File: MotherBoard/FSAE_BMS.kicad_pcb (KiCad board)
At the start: 2 copper layers, 61 parts, among them IC501 BQ79600PWRQ1, J1 DM3AT-SF-PEJM5_40_, J201 Conn_ARM_SWD_TagConnect_TC2030, J301 1376357-3, U201 STM32F205RBTx, U401 LMR51430, U402 LMR51430, U601 PTCAN1462DRQ1, U602 PTCAN1462DRQ1, Y201 16 Mhz

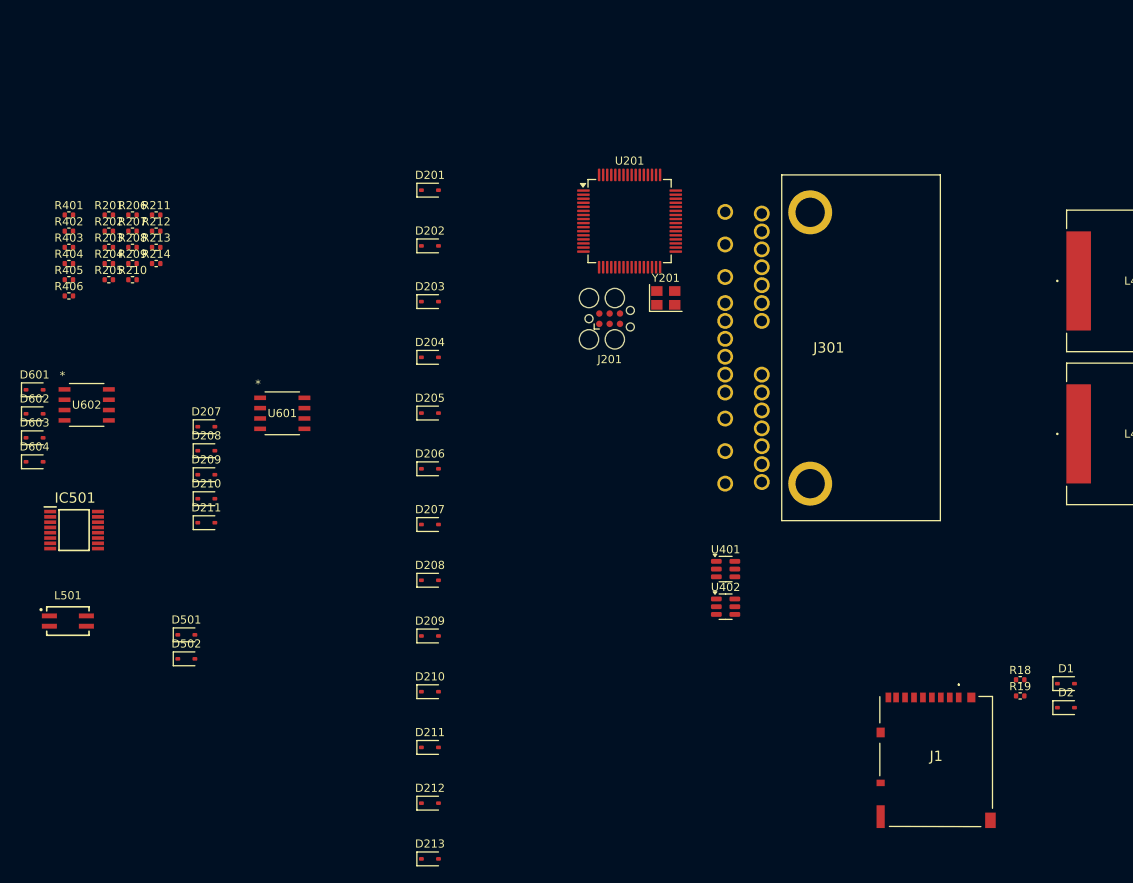
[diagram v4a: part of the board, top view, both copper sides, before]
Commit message: Revised all schematics + completed relay driver page
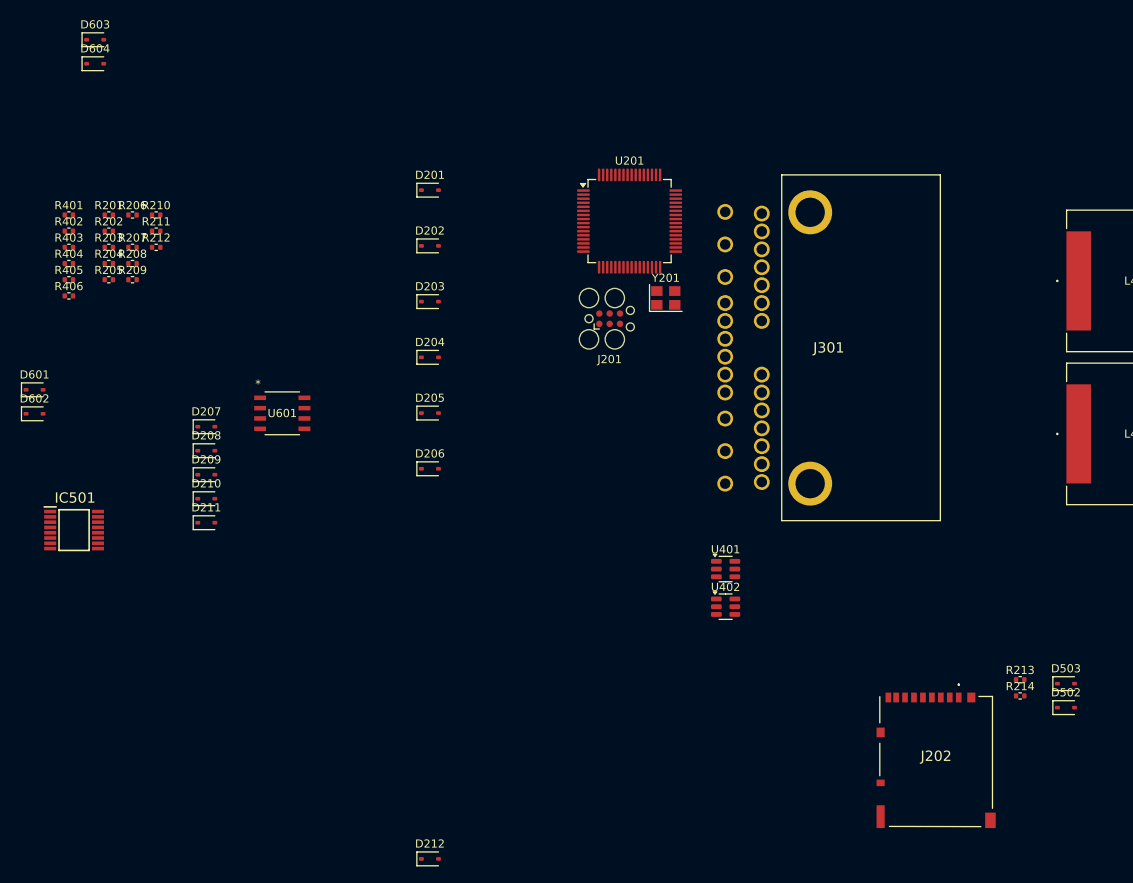
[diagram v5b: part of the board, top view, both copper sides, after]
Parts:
- removed the D207 at (89.1, 88.1)
- removed the D208 at (89.1, 95.0)
- removed the D209 at (89.1, 101.8)
- removed the D210 at (89.1, 108.7)
- removed the D211 at (89.1, 115.5)
- removed the D212 at (89.1, 122.4)
- removed D501: D_TVS, Diode_SMD:D_SOD-323
- removed the D502 at (59.2, 104.7)
- removed L501: WE-SLM, Transformer_WURTH:Isolation_Transformer
- removed the R207 at (52.5, 52.1)
- removed the R214 at (55.5, 56.1)
- removed U602: PTCAN1462DRQ1, TCAN:TCAN
- moved D603 49.5 mm to (48.0, 28.6)
- moved D604 49.5 mm to (48.0, 31.5)
- renumbered D213 to D212, D2 to D502, D1 to D503, J1 to J202, R208 to R207, R209 to R208, R210 to R209, R211 to R210, R212 to R211, R213 to R212, R18 to R213, R19 to R214
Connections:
- net Net-(U601-CANH) renamed /TCAN1462-Q1/CANH_1
- net Net-(U601-CANL) renamed /TCAN1462-Q1/CANL_1
- D502 pad 1: Net-(D1-A2) -> GND
- D503 pad 2: Net-(D1-A2) -> GND
- D601 pad 2: CAN1_CONN+ -> ISO_CAN1+
- D602 pad 1: CAN1_CONN- -> ISO_CAN1-
- D603 pad 2: CAN2_CONN+ -> ISO_CAN2+
- D604 pad 1: CAN2_CONN- -> ISO_CAN2-
- U201 pad 2: unconnected-(U201-PC13-Pad2) -> /MCU/SDIO_DET
- U201 pad 33: unconnected-(U201-PB12-Pad33) -> CAN2_RX
- U201 pad 34: unconnected-(U201-PB13-Pad34) -> CAN2_TX
- U201 pad 44: unconnected-(U201-PA11-Pad44) -> CAN1_RX
- U201 pad 45: unconnected-(U201-PA12-Pad45) -> CAN1_TX
- U201 pad 57: CAN2_RX -> unconnected-(U201-PB5-Pad57)
- U201 pad 58: CAN2_TX -> unconnected-(U201-PB6-Pad58)
- U201 pad 61: CAN1_RX -> unconnected-(U201-PB8-Pad61)
- U201 pad 62: CAN1_TX -> unconnected-(U201-PB9-Pad62)
- U601 pad 1: CAN1_TX -> Net-(U601-TXD)
- U601 pad 4: CAN1_RX -> Net-(U601-RXD)

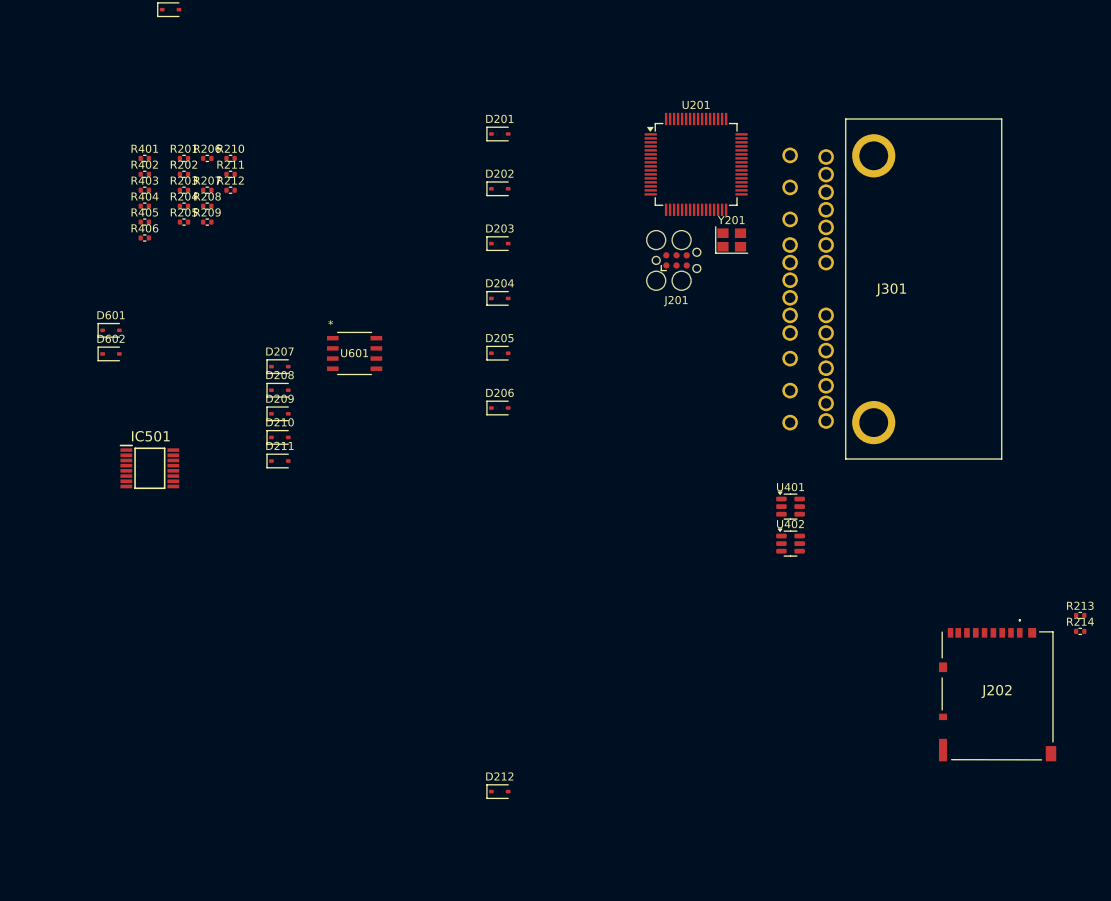
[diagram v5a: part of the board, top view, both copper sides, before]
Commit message: Fixed 3D model paths. Finished PSU ORing shcematic.
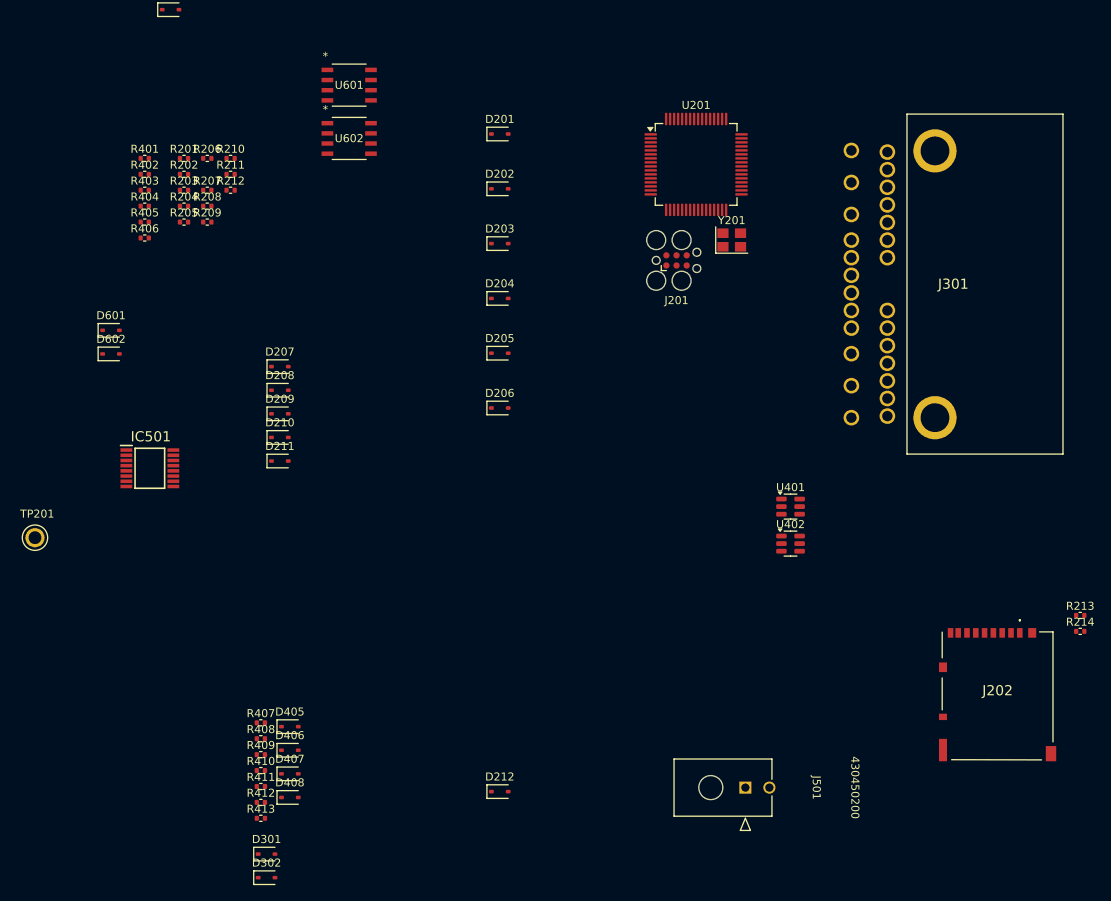
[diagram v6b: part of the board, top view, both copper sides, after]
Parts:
- added D301: D_TVS, Diode_SMD:D_SOD-323, F.Cu at (60.0, 137.1)
- added D302: D_TVS, Diode_SMD:D_SOD-323, F.Cu at (60.0, 140.0)
- added D405: D_TVS, Diode_SMD:D_SOD-323, F.Cu at (62.9, 121.1)
- added D406: D_TVS, Diode_SMD:D_SOD-323, F.Cu at (62.9, 124.1)
- added D407: D_TVS, Diode_SMD:D_SOD-323, F.Cu at (62.9, 127.0)
- added D408: D_TVS, Diode_SMD:D_SOD-323, F.Cu at (62.9, 130.0)
- added J501: 430450200, molex_comm:CON_430450200_MOL, F.Cu at (119.8, 128.7)
- added R407: 100k, Resistor_SMD:R_0402_1005Metric, F.Cu at (59.2, 120.6)
- added R408: 33k, Resistor_SMD:R_0402_1005Metric, F.Cu at (59.2, 122.6)
- added R409: 100k, Resistor_SMD:R_0402_1005Metric, F.Cu at (59.2, 124.6)
- added R410: 33k, Resistor_SMD:R_0402_1005Metric, F.Cu at (59.2, 126.6)
- added R411: 1k, Resistor_SMD:R_0402_1005Metric, F.Cu at (59.2, 128.6)
- added R412: 1k, Resistor_SMD:R_0402_1005Metric, F.Cu at (59.2, 130.6)
- added R413: 1K, Resistor_SMD:R_0402_1005Metric, F.Cu at (59.2, 132.6)
- added TP201: TestPoint, TestPoint:TP_5012, F.Cu at (31.0, 97.5)
- added U602: PTCAN1462DRQ1, CAN1462:CAN1462, F.Cu at (70.3, 47.6)
- U601: footprint TCAN:TCAN -> CAN1462:CAN1462
- moved U601 33.5 mm to (70.3, 40.9)
- moved J301 7.68 mm to (133.1, 49.1)
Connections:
- net CHARGE_EN_CONN renamed CHARGE_EN_HV
- net CHARGE_PWR_CONN renamed CHARGE_PWR
- net CHARGE_SAFE_CONN renamed CHARGE_SAFE_HV
- net DISCHARGE_EN_CONN renamed DISCHARGE_EN_HV
- net FAN_EN renamed FAN_EN_LV
- net FAN_EN_CONN renamed FAN_EN_HV
- net READY_PWR_CONN renamed READY_PWR
- J301 pad 18: CAN1_CONN+ -> ISO_CAN1+
- J301 pad 19: CAN1_CONN- -> ISO_CAN1-
- J301 pad 20: CAN2_CONN- -> ISO_CAN2+
- J301 pad 21: CAN2_CONN+ -> ISO_CAN2-
- J301 pad 24: FAN_PWM_CONN -> unconnected-(J301-Pad24)
- U201 pad 14: ADC3_IN0 -> unconnected-(U201-PA0-Pad14)
- U201 pad 15: ADC3_IN1 -> unconnected-(U201-PA1-Pad15)
- U201 pad 27: CHARGE_PWR_CTRL -> CHARGE_PWR_LV_ISO
- U201 pad 28: READY_PWR_CTRL -> READY_PWR_LV_ISO

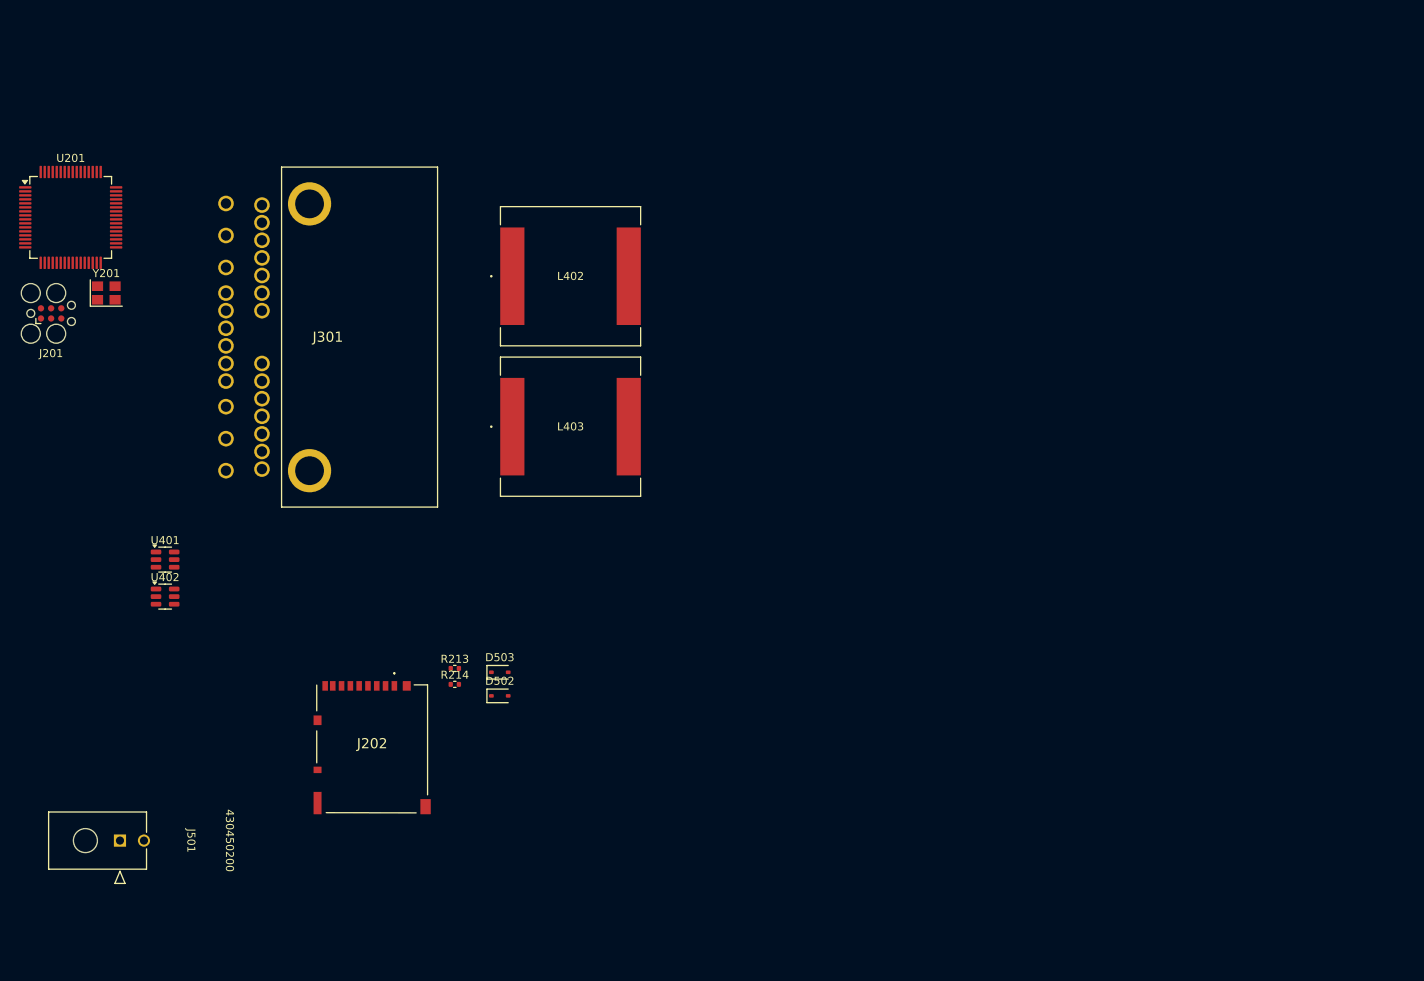
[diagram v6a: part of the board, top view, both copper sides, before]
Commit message: Added more 3D models
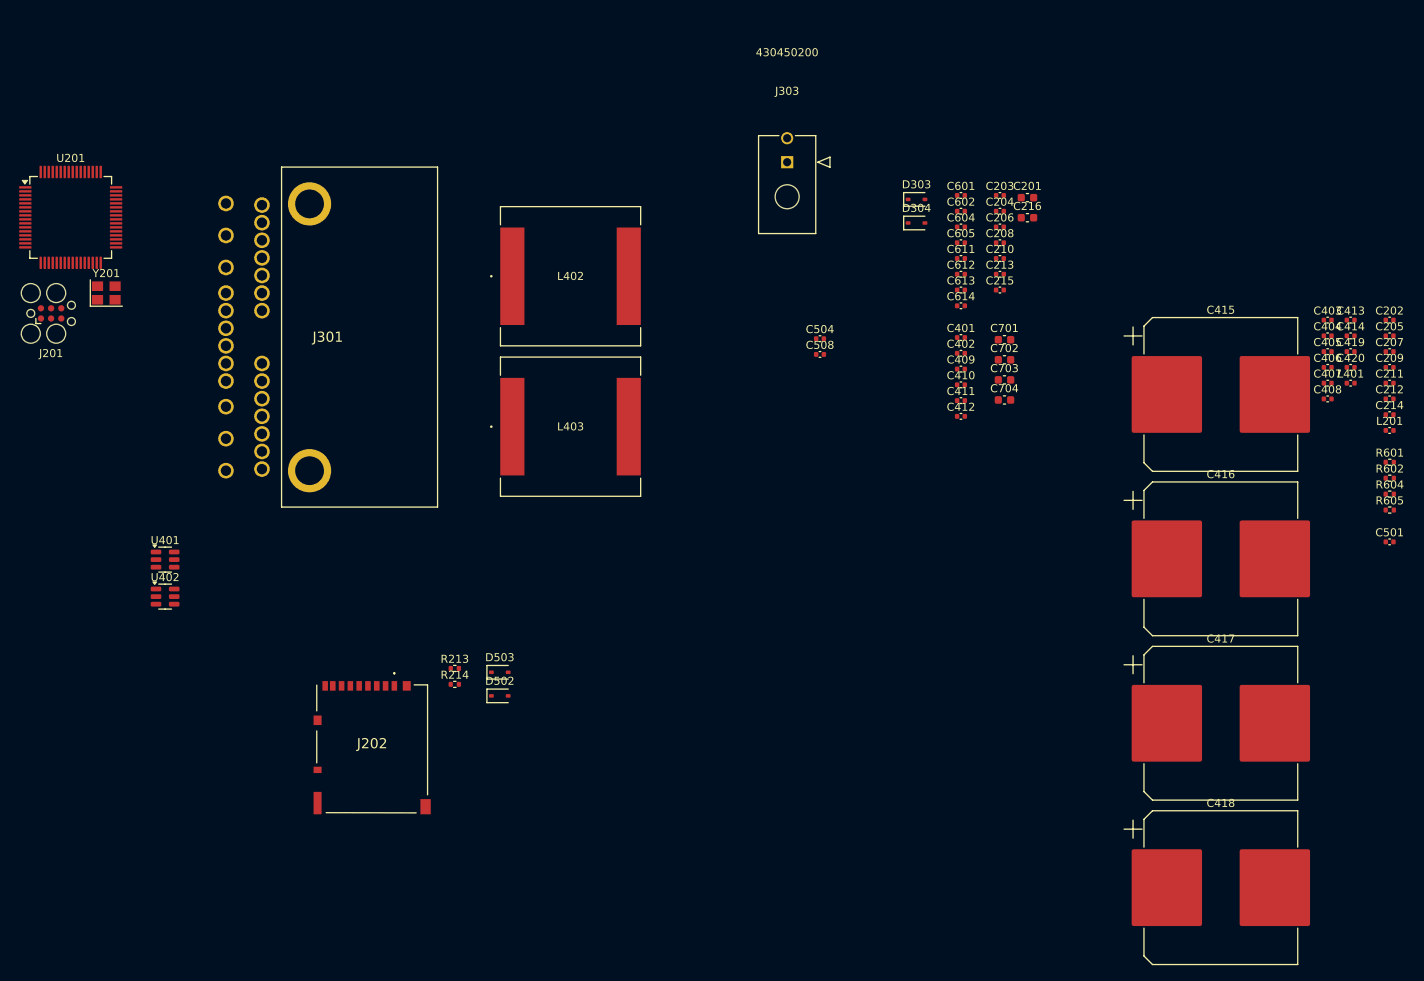
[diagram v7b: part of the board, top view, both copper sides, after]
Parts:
- removed J501: 430450200, molex_comm:CON_430450200_MOL
- added C201: 10u, Capacitor_SMD:C_0603_1608Metric, F.Cu at (233.2, 48.4)
- added C202: 10p, Capacitor_SMD:C_0402_1005Metric, F.Cu at (278.5, 63.7)
- added C203: 100n, Capacitor_SMD:C_0402_1005Metric, F.Cu at (229.8, 48.1)
- added C204: 100n, Capacitor_SMD:C_0402_1005Metric, F.Cu at (229.8, 50.1)
- added C205: 10p, Capacitor_SMD:C_0402_1005Metric, F.Cu at (278.5, 65.7)
- added C206: 100n, Capacitor_SMD:C_0402_1005Metric, F.Cu at (229.8, 52.0)
- added C207: 2u2, Capacitor_SMD:C_0402_1005Metric, F.Cu at (278.5, 67.6)
- added C208: 100n, Capacitor_SMD:C_0402_1005Metric, F.Cu at (229.8, 54.0)
- added C209: 2u2, Capacitor_SMD:C_0402_1005Metric, F.Cu at (278.5, 69.6)
- added C210: 100n, Capacitor_SMD:C_0402_1005Metric, F.Cu at (229.8, 56.0)
- added C211: 10n, Capacitor_SMD:C_0402_1005Metric, F.Cu at (278.5, 71.6)
- added C212: 1u, Capacitor_SMD:C_0402_1005Metric, F.Cu at (278.5, 73.5)
- added C213: 100n, Capacitor_SMD:C_0402_1005Metric, F.Cu at (229.8, 58.0)
- added C214: 1u, Capacitor_SMD:C_0402_1005Metric, F.Cu at (278.5, 75.5)
- added C215: 100n, Capacitor_SMD:C_0402_1005Metric, F.Cu at (229.8, 59.9)
- added C216: 10u, Capacitor_SMD:C_0603_1608Metric, F.Cu at (233.2, 50.9)
- added C401: 100n, Capacitor_SMD:C_0402_1005Metric, F.Cu at (224.9, 65.9)
- added C402: 100n, Capacitor_SMD:C_0402_1005Metric, F.Cu at (224.9, 67.8)
- added C403: 1u, Capacitor_SMD:C_0402_1005Metric, F.Cu at (270.8, 63.7)
- added C404: 1u, Capacitor_SMD:C_0402_1005Metric, F.Cu at (270.8, 65.7)
- added C405: 1u, Capacitor_SMD:C_0402_1005Metric, F.Cu at (270.8, 67.6)
- added C406: 1u, Capacitor_SMD:C_0402_1005Metric, F.Cu at (270.8, 69.6)
- added C407: 1u, Capacitor_SMD:C_0402_1005Metric, F.Cu at (270.8, 71.6)
- added C408: 1u, Capacitor_SMD:C_0402_1005Metric, F.Cu at (270.8, 73.5)
- added C409: 100n, Capacitor_SMD:C_0402_1005Metric, F.Cu at (224.9, 69.8)
- added C410: 100n, Capacitor_SMD:C_0402_1005Metric, F.Cu at (224.9, 71.8)
- added C411: 100n, Capacitor_SMD:C_0402_1005Metric, F.Cu at (224.9, 73.7)
- added C412: 100n, Capacitor_SMD:C_0402_1005Metric, F.Cu at (224.9, 75.7)
- added C413: 47u, Capacitor_SMD:C_0402_1005Metric, F.Cu at (273.6, 63.7)
- added C414: 47u, Capacitor_SMD:C_0402_1005Metric, F.Cu at (273.6, 65.7)
- added C415: 3300u, Capacitor_SMD:CP_Elec_18x17.5, F.Cu at (257.4, 73.0)
- added C416: 3300u, Capacitor_SMD:CP_Elec_18x17.5, F.Cu at (257.4, 93.5)
- added C417: 3300u, Capacitor_SMD:CP_Elec_18x17.5, F.Cu at (257.4, 114.1)
- added C418: 3300u, Capacitor_SMD:CP_Elec_18x17.5, F.Cu at (257.4, 134.6)
- added C419: 10n, Capacitor_SMD:C_0402_1005Metric, F.Cu at (273.6, 67.6)
- added C420: 10n, Capacitor_SMD:C_0402_1005Metric, F.Cu at (273.6, 69.6)
- added C501: 10n, Capacitor_SMD:C_0402_1005Metric, F.Cu at (278.5, 91.4)
- added C504: 100n, Capacitor_SMD:C_0402_1005Metric, F.Cu at (207.3, 66.0)
- added C508: 100n, Capacitor_SMD:C_0402_1005Metric, F.Cu at (207.3, 68.0)
- added C601: 100n, Capacitor_SMD:C_0402_1005Metric, F.Cu at (224.9, 48.1)
- added C602: 100n, Capacitor_SMD:C_0402_1005Metric, F.Cu at (224.9, 50.1)
- added C604: 100n, Capacitor_SMD:C_0402_1005Metric, F.Cu at (224.9, 52.0)
- added C605: 100n, Capacitor_SMD:C_0402_1005Metric, F.Cu at (224.9, 54.0)
- added C611: 100n, Capacitor_SMD:C_0402_1005Metric, F.Cu at (224.9, 56.0)
- added C612: 100n, Capacitor_SMD:C_0402_1005Metric, F.Cu at (224.9, 58.0)
- added C613: 100n, Capacitor_SMD:C_0402_1005Metric, F.Cu at (224.9, 59.9)
- added C614: 100n, Capacitor_SMD:C_0402_1005Metric, F.Cu at (224.9, 61.9)
- added C701: 10u, Capacitor_SMD:C_0603_1608Metric, F.Cu at (230.4, 66.1)
- added C702: 10u, Capacitor_SMD:C_0603_1608Metric, F.Cu at (230.4, 68.6)
- added C703: 10u, Capacitor_SMD:C_0603_1608Metric, F.Cu at (230.4, 71.2)
- added C704: 10u, Capacitor_SMD:C_0603_1608Metric, F.Cu at (230.4, 73.7)
- added D303: D_TVS, Diode_SMD:D_SOD-323, F.Cu at (219.4, 48.6)
- added D304: D_TVS, Diode_SMD:D_SOD-323, F.Cu at (219.4, 51.5)
- added J303: 430450200, molex_comm:CON_430450200_MOL, F.Cu at (203.2, 43.9)
- added L201: 10n, Capacitor_SMD:C_0402_1005Metric, F.Cu at (278.5, 77.5)
- added L401: 10n, Capacitor_SMD:C_0402_1005Metric, F.Cu at (273.6, 71.6)
- added R601: 0, Resistor_SMD:R_0402_1005Metric, F.Cu at (278.5, 81.5)
- added R602: 0, Resistor_SMD:R_0402_1005Metric, F.Cu at (278.5, 83.4)
- added R604: 0, Resistor_SMD:R_0402_1005Metric, F.Cu at (278.5, 85.4)
- added R605: 0, Resistor_SMD:R_0402_1005Metric, F.Cu at (278.5, 87.4)
